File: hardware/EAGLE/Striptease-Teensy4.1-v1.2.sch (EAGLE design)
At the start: 11 parts

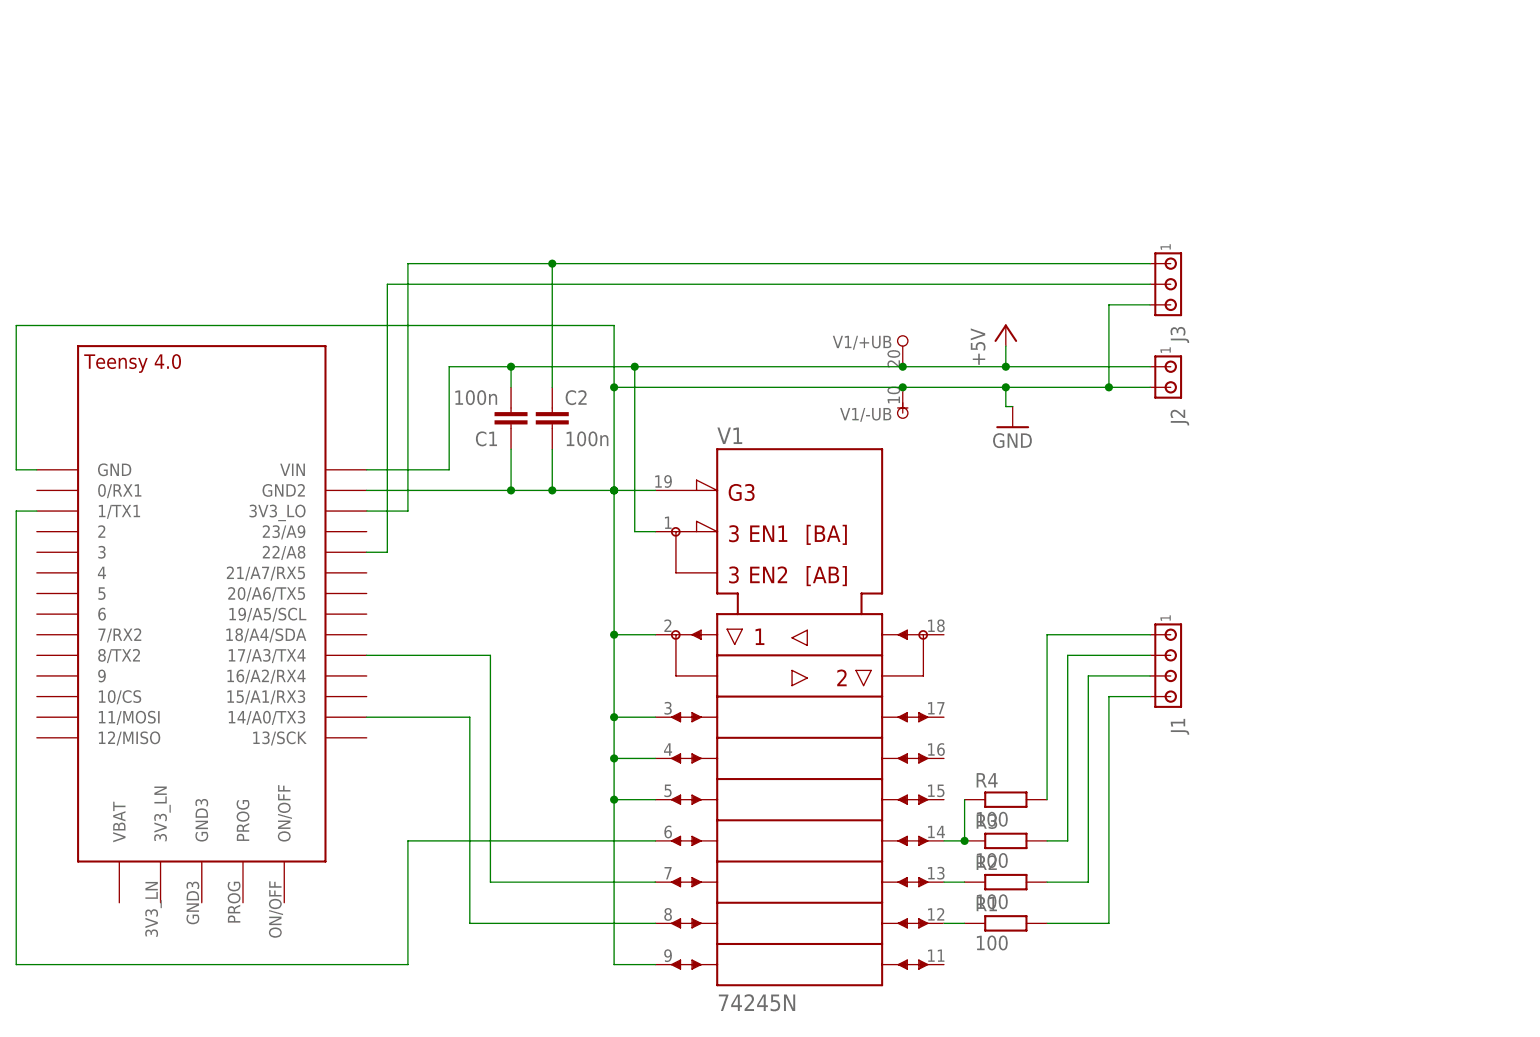
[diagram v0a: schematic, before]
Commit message: Change connector names in EAGLE boards.
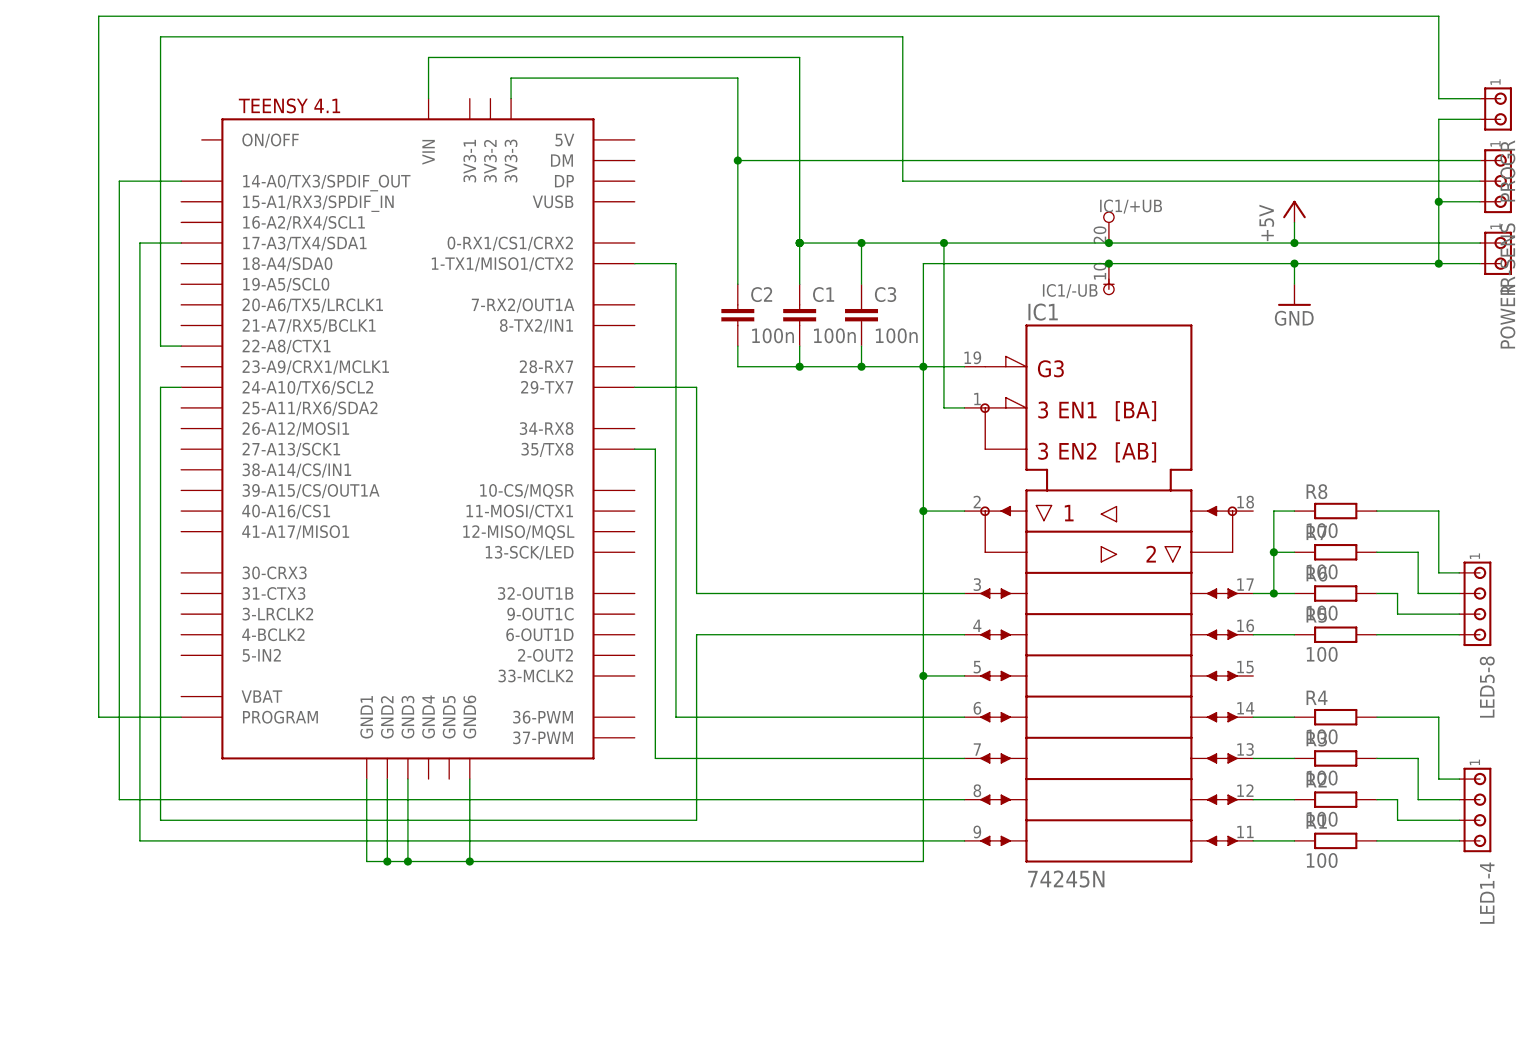
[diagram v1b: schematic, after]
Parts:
- removed J1: (no value), con-amp:MTA04-100
- removed J2: (no value), con-amp:MTA02-100
- removed J3: (no value), con-amp:MTA03-100
- removed U$1: TEENSY_4.0-BASIC, Teensy-4.0:TEENSY_4.0-BASIC
- removed V1: 74245N, 74ttl-din:74245N
- added C3: 100n, rcl:C-EU050-025X075
- added IC1: 74245N, 74ttl-din:74245N
- added IR-SENS: (no value), con-amp:MTA03-100
- added LED1-4, LED5-8: (no value), con-amp:MTA04-100
- added POWER, PROGR: (no value), con-amp:MTA02-100
- added R5, R6, R7, R8: 100, rcl:R-EU_0207/10
- added U$3: TEENSY41-E, teensy:TEENSY41-E
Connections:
- removed net N$21: U$1.1/TX1, V11.A5
- removed net N$5: J1.1, R4.2
- new net N$16: IC11.B5, R4.1
- new net N$19: LED1-4.1, R4.2
- new net N$20: LED5-8.4, R5.2
- new net N$22: LED5-8.3, R6.2
- new net N$23: IC11.A8, U$3.17-A3/TX4/SDA1
- new net N$24: IC11.A7, U$3.14-A0/TX3/SPDIF_OUT
- new net N$25: IC11.A6, U$3.35/TX8
- new net N$26: IC11.A5, U$3.1-TX1/MISO1/CTX2
- new net N$27: IC11.A3, U$3.24-A10/TX6/SCL2
- new net N$28: IC11.A2, U$3.29-TX7
- new net N$3: IC11.B3, R5.1
- new net N$31: IR-SENS.2, U$3.22-A8/CTX1
- new net N$6: LED5-8.2, R7.2
- net +5V: now also C1.1, C3.1, IC1/+UB.+UB, IC11.DIR, POWER.1, U$3.VIN; no longer C1.2, J2.1, U$1.VIN, V1/+UB.+UB, V11.DIR
- net GND: now also C1.2, C3.2, IC1/-UB.-UB, IC11.!G, IC11.A1, IC11.A4, IR-SENS.3, POWER.2, PROGR.2, U$3.GND1, U$3.GND2, U$3.GND3, U$3.GND6; no longer C1.1, J2.2, J3.3, U$1.GND, U$1.GND2, V1/-UB.-UB, V11.!G, V11.A1, V11.A2, V11.A3, V11.A4, V11.A8
- net N$1: now also C2.1, IR-SENS.1, U$3.3V3-3; no longer J3.2, U$1.22/A8
- net N$10: now also LED5-8.1, R8.2; no longer U$1.14/A0/TX3, V11.A7
- net N$11: now also IC11.B8; no longer V11.B7
- net N$12: now also IC11.B7; no longer V11.B6
- net N$13: now also IC11.B6; no longer R4.1, V11.B5
- net N$14: now also IC11.B2, R6.1, R7.1, R8.1; no longer U$1.17/A3/TX4, V11.A6
- net N$2: now also PROGR.1, U$3.PROGRAM; no longer C2.1, J3.1, U$1.3V3_LO
- net N$7: now also LED1-4.2; no longer J1.2
- net N$8: now also LED1-4.3; no longer J1.3
- net N$9: now also LED1-4.4; no longer J1.4
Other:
- moved on the sheet: C1, C2, R1, R2, R3, R4

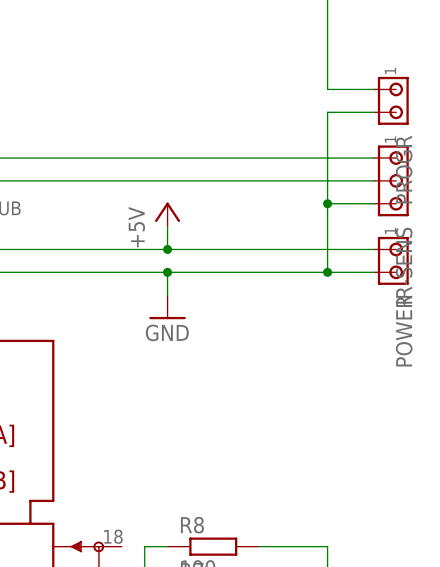
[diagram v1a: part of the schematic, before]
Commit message: Add connector pinout for LEDs in EAGLE boards.
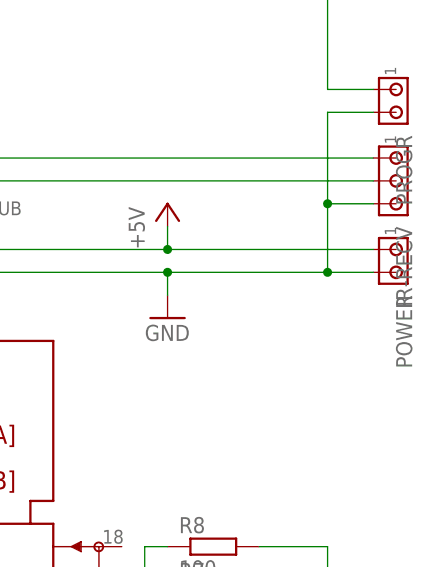
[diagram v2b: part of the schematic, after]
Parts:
- renumbered IR-SENS to IR-RECV
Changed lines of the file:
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@@
 <part name="U$3" library="teensy" deviceset="TEENSY41-E" device=""/>
 <part name="C3" library="rcl" library_urn="urn:adsk.eagle:library:334" deviceset="C-EU" device="050-025X075" package3d_urn="urn:adsk.eagle:package:23637/1" value="100n"/>
-<part name="IR-SENS" library="con-amp" library_urn="urn:adsk.eagle:library:127" deviceset="MTA03-100" device="" package3d_urn="urn:adsk.eagle:package:8081621/1"/>
+<part name="IR-RECV" library="con-amp" library_urn="urn:adsk.eagle:library:127" deviceset="MTA03-100" device="" package3d_urn="urn:adsk.eagle:package:8081621/1"/>
 <part name="PROGR" library="con-amp" library_urn="urn:adsk.eagle:library:127" deviceset="MTA02-100" device="" package3d_urn="urn:adsk.eagle:package:8081649/1"/>
 </parts>
@@
 <attribute name="VALUE" x="110.744" y="81.661" size="1.778" layer="96"/>
 </instance>
-<instance part="IR-SENS" gate="G$1" x="187.96" y="101.6" smashed="yes" rot="R270">
+<instance part="IR-RECV" gate="G$1" x="187.96" y="101.6" smashed="yes" rot="R270">
 <attribute name="NAME" x="187.96" y="96.52" size="1.778" layer="95" rot="R270"/>
 <attribute name="VALUE" x="184.15" y="96.52" size="1.778" layer="96" rot="R270"/>
@@
 <pinref part="U$3" gate="G$1" pin="22-A8/CTX1"/>
 <wire x1="25.4" y1="81.28" x2="22.86" y2="81.28" width="0.1524" layer="91"/>
-<pinref part="IR-SENS" gate="G$1" pin="2"/>
+<pinref part="IR-RECV" gate="G$1" pin="2"/>
 <wire x1="114.3" y1="101.6" x2="185.42" y2="101.6" width="0.1524" layer="91"/>
 </segment>
@@
 <wire x1="66.04" y1="114.3" x2="66.04" y2="111.76" width="0.1524" layer="91"/>
 <wire x1="93.98" y1="114.3" x2="93.98" y2="104.14" width="0.1524" layer="91"/>
-<pinref part="IR-SENS" gate="G$1" pin="1"/>
+<pinref part="IR-RECV" gate="G$1" pin="1"/>
 <wire x1="93.98" y1="104.14" x2="93.98" y2="88.9" width="0.1524" layer="91"/>
 <wire x1="185.42" y1="104.14" x2="93.98" y2="104.14" width="0.1524" layer="91"/>
@@
 <wire x1="162.56" y1="91.44" x2="139.7" y2="91.44" width="0.1524" layer="91"/>
 <pinref part="POWER" gate="G$1" pin="2"/>
-<pinref part="IR-SENS" gate="G$1" pin="3"/>
+<pinref part="IR-RECV" gate="G$1" pin="3"/>
 <wire x1="185.42" y1="99.06" x2="180.34" y2="99.06" width="0.1524" layer="91"/>
 <pinref part="PROGR" gate="G$1" pin="2"/>
